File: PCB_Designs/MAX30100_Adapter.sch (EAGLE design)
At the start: 15 parts

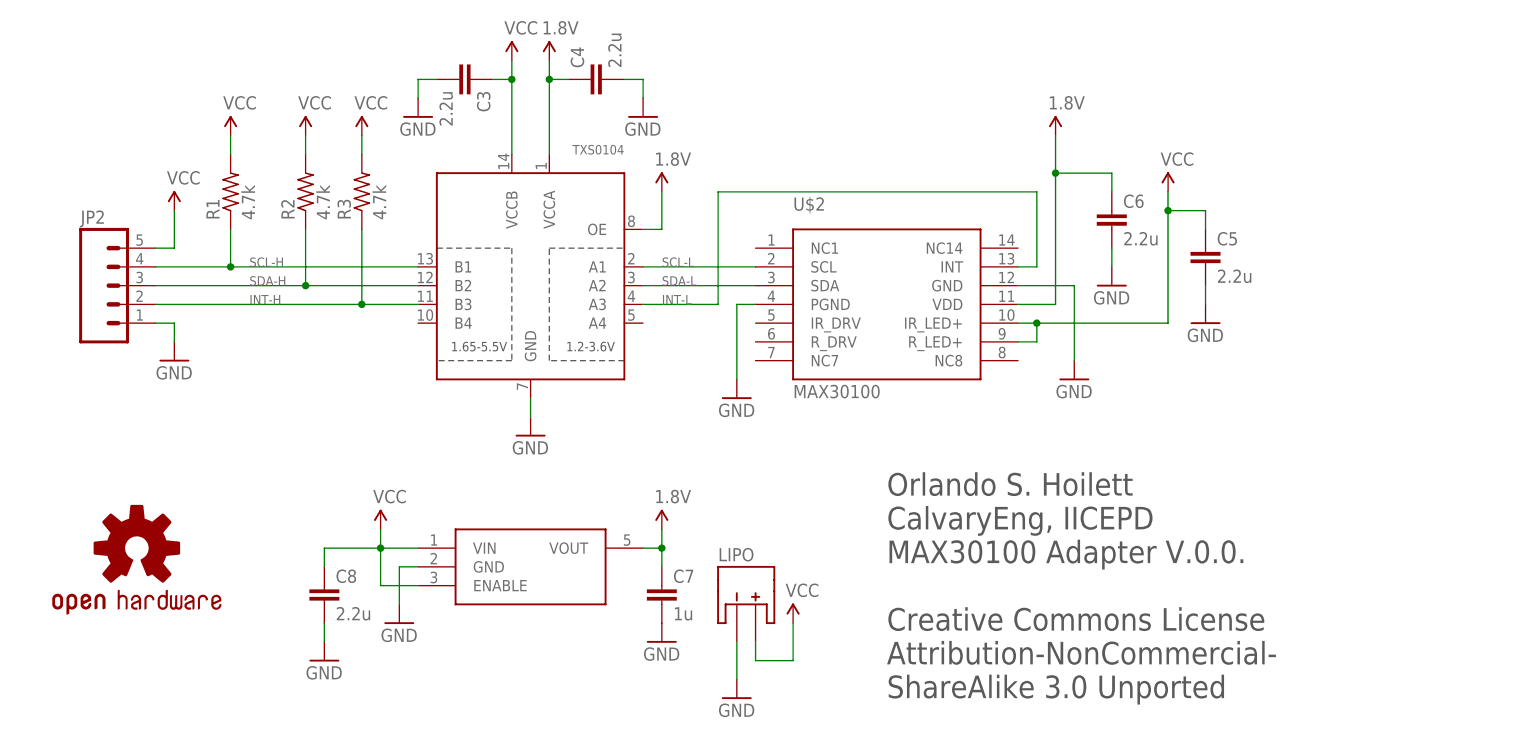
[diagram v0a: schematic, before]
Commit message: first version of PCB sent to OSHPark
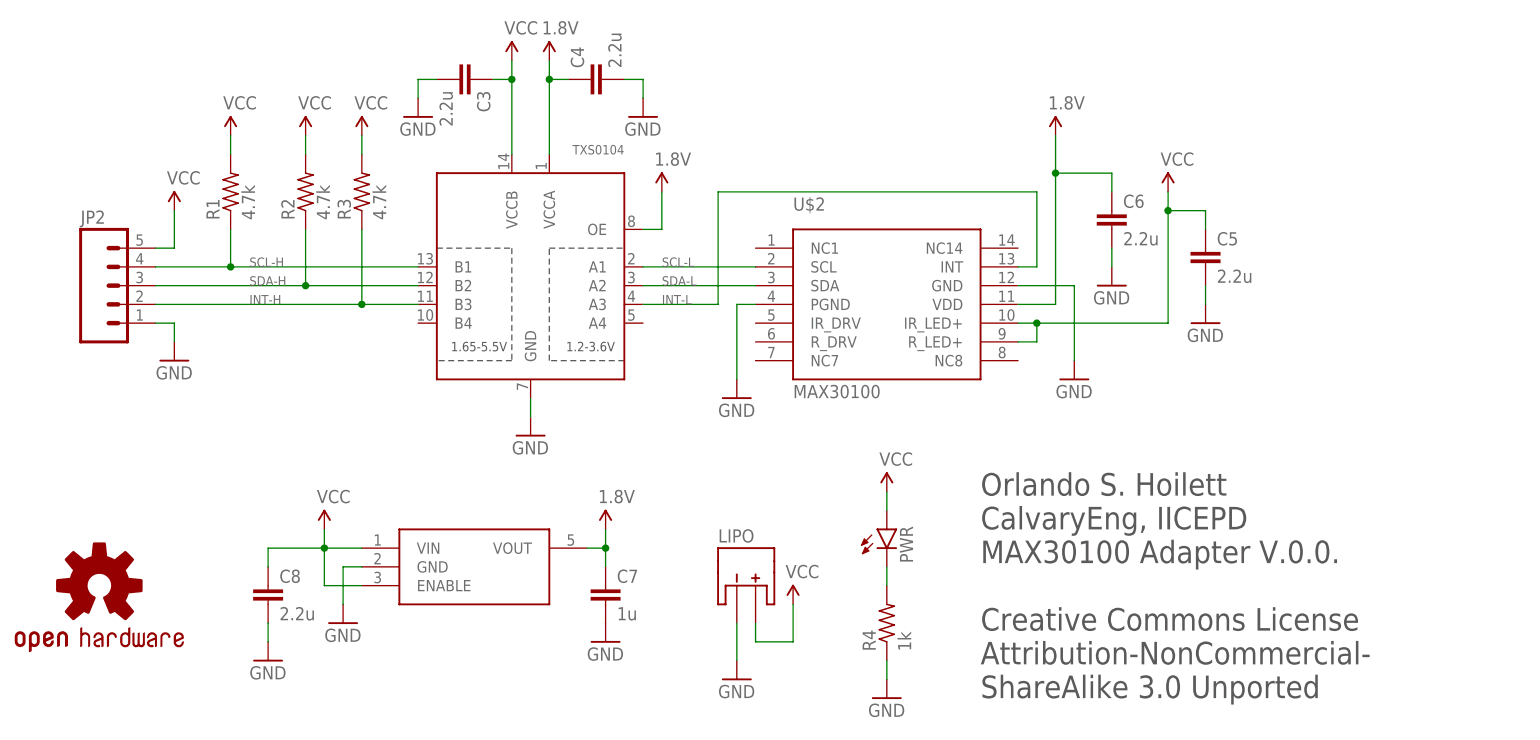
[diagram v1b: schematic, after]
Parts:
- added PWR: (no value), SparkFun-LED:LED0603
- added R4: 1k, resistor:R-US_R0402
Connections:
- new net N$1: PWR.C, R4.2
- net GND: now also R4.1
- net VCC: now also PWR.A
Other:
- moved on the sheet: C7, C8, LIPO
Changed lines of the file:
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@@
 <part name="GND14" library="SparkFun-Aesthetics" deviceset="GND" device=""/>
 <part name="LOGO1" library="SparkFun-Aesthetics" deviceset="OSHW-LOGO" device="S"/>
+<part name="PWR" library="SparkFun-LED" deviceset="LED" device="0603"/>
+<part name="R4" library="resistor" deviceset="R-US_" device="R0402" value="1k"/>
+<part name="GND1" library="SparkFun-Aesthetics" deviceset="GND" device=""/>
+<part name="SUPPLY1" library="SparkFun-Aesthetics" deviceset="VCC" device=""/>
 </parts>
 <sheets>
 <sheet>
 <plain>
-<text x="162.56" y="-7.62" size="3.048" layer="97">Orlando S. Hoilett
+<text x="175.26" y="-7.62" size="3.048" layer="97">Orlando S. Hoilett
 CalvaryEng, IICEPD
 MAX30100 Adapter V.0.0.
@@
 <wire x1="137.16" y1="86.36" x2="137.16" y2="27.94" width="0.508" layer="90" style="shortdash"/>
 <wire x1="137.16" y1="27.94" x2="137.16" y2="22.86" width="0.508" layer="90" style="shortdash"/>
-<wire x1="137.16" y1="22.86" x2="78.74" y2="22.86" width="0.508" layer="90" style="shortdash"/>
-<wire x1="78.74" y1="22.86" x2="48.26" y2="22.86" width="0.508" layer="90" style="shortdash"/>
+<wire x1="137.16" y1="22.86" x2="68.58" y2="22.86" width="0.508" layer="90" style="shortdash"/>
+<wire x1="68.58" y1="22.86" x2="48.26" y2="22.86" width="0.508" layer="90" style="shortdash"/>
 <wire x1="48.26" y1="22.86" x2="48.26" y2="86.36" width="0.508" layer="90" style="shortdash"/>
 <text x="63.5" y="88.9" size="4.064" layer="90">Level Shift</text>
 <wire x1="137.16" y1="86.36" x2="215.9" y2="86.36" width="0.508" layer="90" style="shortdash"/>
 <wire x1="215.9" y1="86.36" x2="215.9" y2="27.94" width="0.508" layer="90" style="shortdash"/>
-<wire x1="215.9" y1="27.94" x2="157.48" y2="27.94" width="0.508" layer="90" style="shortdash"/>
+<wire x1="215.9" y1="27.94" x2="172.72" y2="27.94" width="0.508" layer="90" style="shortdash"/>
 <text x="144.78" y="76.2" size="4.064" layer="90">MAX30100</text>
-<wire x1="157.48" y1="27.94" x2="137.16" y2="27.94" width="0.508" layer="90" style="shortdash"/>
-<wire x1="78.74" y1="22.86" x2="78.74" y2="-12.7" width="0.508" layer="90" style="shortdash"/>
-<wire x1="78.74" y1="-12.7" x2="157.48" y2="-12.7" width="0.508" layer="90" style="shortdash"/>
-<wire x1="157.48" y1="-12.7" x2="157.48" y2="27.94" width="0.508" layer="90" style="shortdash"/>
+<wire x1="172.72" y1="27.94" x2="137.16" y2="27.94" width="0.508" layer="90" style="shortdash"/>
+<wire x1="68.58" y1="22.86" x2="68.58" y2="-12.7" width="0.508" layer="90" style="shortdash"/>
+<wire x1="68.58" y1="-12.7" x2="172.72" y2="-12.7" width="0.508" layer="90" style="shortdash"/>
+<wire x1="172.72" y1="-12.7" x2="172.72" y2="27.94" width="0.508" layer="90" style="shortdash"/>
 <text x="83.82" y="-17.78" size="4.064" layer="90">Battery and Regulator</text>
 </plain>
@@
 <instance part="GND10" gate="1" x="193.04" y="48.26"/>
 <instance part="SUPPLY6" gate="G$1" x="185.42" y="68.58"/>
-<instance part="LIPO" gate="G$1" x="144.78" y="5.08"/>
+<instance part="LIPO" gate="G$1" x="144.78" y="7.62"/>
 <instance part="R1" gate="G$1" x="73.66" y="60.96" rot="R90"/>
 <instance part="R2" gate="G$1" x="83.82" y="60.96" rot="R90"/>
@@
 <instance part="SUPPLY10" gate="G$1" x="83.82" y="68.58"/>
 <instance part="SUPPLY11" gate="G$1" x="91.44" y="68.58"/>
-<instance part="GND11" gate="1" x="142.24" y="-7.62"/>
-<instance part="SUPPLY12" gate="G$1" x="149.86" y="2.54"/>
-<instance part="LDO" gate="G$1" x="114.3" y="10.16"/>
-<instance part="C7" gate="G$1" x="132.08" y="7.62"/>
-<instance part="GND12" gate="1" x="132.08" y="0"/>
-<instance part="SUPPLY13" gate="G$1" x="132.08" y="15.24"/>
-<instance part="SUPPLY14" gate="G$1" x="93.98" y="15.24"/>
-<instance part="GND13" gate="1" x="96.52" y="2.54"/>
-<instance part="C8" gate="G$1" x="86.36" y="7.62"/>
-<instance part="GND14" gate="1" x="86.36" y="-2.54"/>
-<instance part="LOGO1" gate="G$1" x="60.96" y="12.7"/>
+<instance part="GND11" gate="1" x="142.24" y="-5.08"/>
+<instance part="SUPPLY12" gate="G$1" x="149.86" y="5.08"/>
+<instance part="LDO" gate="G$1" x="106.68" y="10.16"/>
+<instance part="C7" gate="G$1" x="124.46" y="7.62"/>
+<instance part="GND12" gate="1" x="124.46" y="0"/>
+<instance part="SUPPLY13" gate="G$1" x="124.46" y="15.24"/>
+<instance part="SUPPLY14" gate="G$1" x="86.36" y="15.24"/>
+<instance part="GND13" gate="1" x="88.9" y="2.54"/>
+<instance part="C8" gate="G$1" x="78.74" y="7.62"/>
+<instance part="GND14" gate="1" x="78.74" y="-2.54"/>
+<instance part="LOGO1" gate="G$1" x="55.88" y="7.62"/>
+<instance part="PWR" gate="G$1" x="162.56" y="15.24"/>
+<instance part="R4" gate="G$1" x="162.56" y="2.54" rot="R90"/>
+<instance part="GND1" gate="1" x="162.56" y="-7.62"/>
+<instance part="SUPPLY1" gate="G$1" x="162.56" y="20.32"/>
 </instances>
 <busses>
@@
 <segment>
 <pinref part="LIPO" gate="G$1" pin="+"/>
-<wire x1="144.78" y1="0" x2="144.78" y2="-2.54" width="0.1524" layer="91"/>
+<wire x1="144.78" y1="2.54" x2="144.78" y2="0" width="0.1524" layer="91"/>
 <pinref part="SUPPLY12" gate="G$1" pin="VCC"/>
-<wire x1="144.78" y1="-2.54" x2="149.86" y2="-2.54" width="0.1524" layer="91"/>
-<wire x1="149.86" y1="-2.54" x2="149.86" y2="2.54" width="0.1524" layer="91"/>
+<wire x1="144.78" y1="0" x2="149.86" y2="0" width="0.1524" layer="91"/>
+<wire x1="149.86" y1="0" x2="149.86" y2="5.08" width="0.1524" layer="91"/>
 </segment>
 <segment>
 <pinref part="LDO" gate="G$1" pin="ENABLE"/>
-<wire x1="99.06" y1="7.62" x2="93.98" y2="7.62" width="0.1524" layer="91"/>
-<wire x1="93.98" y1="7.62" x2="93.98" y2="12.7" width="0.1524" layer="91"/>
+<wire x1="91.44" y1="7.62" x2="86.36" y2="7.62" width="0.1524" layer="91"/>
+<wire x1="86.36" y1="7.62" x2="86.36" y2="12.7" width="0.1524" layer="91"/>
 <pinref part="LDO" gate="G$1" pin="VIN"/>
-<wire x1="93.98" y1="12.7" x2="99.06" y2="12.7" width="0.1524" layer="91"/>
+<wire x1="86.36" y1="12.7" x2="91.44" y2="12.7" width="0.1524" layer="91"/>
 <pinref part="SUPPLY14" gate="G$1" pin="VCC"/>
-<wire x1="93.98" y1="15.24" x2="93.98" y2="12.7" width="0.1524" layer="91"/>
-<junction x="93.98" y="12.7"/>
+<wire x1="86.36" y1="15.24" x2="86.36" y2="12.7" width="0.1524" layer="91"/>
+<junction x="86.36" y="12.7"/>
 <pinref part="C8" gate="G$1" pin="1"/>
-<wire x1="86.36" y1="10.16" x2="86.36" y2="12.7" width="0.1524" layer="91"/>
-<wire x1="86.36" y1="12.7" x2="93.98" y2="12.7" width="0.1524" layer="91"/>
+<wire x1="78.74" y1="10.16" x2="78.74" y2="12.7" width="0.1524" layer="91"/>
+<wire x1="78.74" y1="12.7" x2="86.36" y2="12.7" width="0.1524" layer="91"/>
+</segment>
+<segment>
+<pinref part="PWR" gate="G$1" pin="A"/>
+<pinref part="SUPPLY1" gate="G$1" pin="VCC"/>
+<wire x1="162.56" y1="20.32" x2="162.56" y2="17.78" width="0.1524" layer="91"/>
 </segment>
 </net>
@@
 <segment>
 <pinref part="LDO" gate="G$1" pin="VOUT"/>
-<wire x1="129.54" y1="12.7" x2="132.08" y2="12.7" width="0.1524" layer="91"/>
-<wire x1="132.08" y1="12.7" x2="132.08" y2="15.24" width="0.1524" layer="91"/>
+<wire x1="121.92" y1="12.7" x2="124.46" y2="12.7" width="0.1524" layer="91"/>
+<wire x1="124.46" y1="12.7" x2="124.46" y2="15.24" width="0.1524" layer="91"/>
 <pinref part="C7" gate="G$1" pin="1"/>
-<wire x1="132.08" y1="10.16" x2="132.08" y2="12.7" width="0.1524" layer="91"/>
-<junction x="132.08" y="12.7"/>
+<wire x1="124.46" y1="10.16" x2="124.46" y2="12.7" width="0.1524" layer="91"/>
+<junction x="124.46" y="12.7"/>
 <pinref part="SUPPLY13" gate="G$1" pin="1.8V"/>
 </segment>
@@
 <pinref part="LIPO" gate="G$1" pin="-"/>
 <pinref part="GND11" gate="1" pin="GND"/>
-<wire x1="142.24" y1="-5.08" x2="142.24" y2="0" width="0.1524" layer="91"/>
+<wire x1="142.24" y1="-2.54" x2="142.24" y2="2.54" width="0.1524" layer="91"/>
 </segment>
 <segment>
@@
 <segment>
 <pinref part="LDO" gate="G$1" pin="GND"/>
-<wire x1="99.06" y1="10.16" x2="96.52" y2="10.16" width="0.1524" layer="91"/>
-<wire x1="96.52" y1="10.16" x2="96.52" y2="5.08" width="0.1524" layer="91"/>
+<wire x1="91.44" y1="10.16" x2="88.9" y2="10.16" width="0.1524" layer="91"/>
+<wire x1="88.9" y1="10.16" x2="88.9" y2="5.08" width="0.1524" layer="91"/>
 <pinref part="GND13" gate="1" pin="GND"/>
 </segment>
@@
 <pinref part="C8" gate="G$1" pin="2"/>
 <pinref part="GND14" gate="1" pin="GND"/>
-<wire x1="86.36" y1="0" x2="86.36" y2="2.54" width="0.1524" layer="91"/>
+<wire x1="78.74" y1="0" x2="78.74" y2="2.54" width="0.1524" layer="91"/>
+</segment>
+<segment>
+<pinref part="R4" gate="G$1" pin="1"/>
+<pinref part="GND1" gate="1" pin="GND"/>
+<wire x1="162.56" y1="-5.08" x2="162.56" y2="-2.54" width="0.1524" layer="91"/>
 </segment>
 </net>
@@
 </segment>
 </net>
+<net name="N$1" class="0">
+<segment>
+<pinref part="PWR" gate="G$1" pin="C"/>
+<pinref part="R4" gate="G$1" pin="2"/>
+<wire x1="162.56" y1="7.62" x2="162.56" y2="10.16" width="0.1524" layer="91"/>
+</segment>
+</net>
